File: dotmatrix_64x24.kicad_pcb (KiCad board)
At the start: 2 copper layers, 165.1 x 91.4 mm, 191 parts, among them CON1 BARREL_JACK, P1 CONN_01X09, P2 CONN_01X09, P3 CONN_01X04, P4 CONN_01X03, Q1 NJL7302L-F3, SW1 SW_PUSH_SMALL_H, SW2 SW_PUSH_SMALL_H, SW3 SW_PUSH_SMALL_H, SW4 SW_PUSH_SMALL_H, SW5 SW_PUSH_SMALL_H, SW6 SW_PUSH_SMALL_H, SW7 SW_PUSH_SMALL_H, SW8 SW_PUSH_SMALL_H, U1 WROOM-02, U10 LED1642GW, U11 LED1642GW, U12 AE-BME280, U2 74HC595-alt-vdd, U3 TD62783, U4 74HC595-alt-vdd, U5 TD62783, U6 LED1642GW, U7 74HC595-alt-vdd, U8 TD62783, U9 LED1642GW

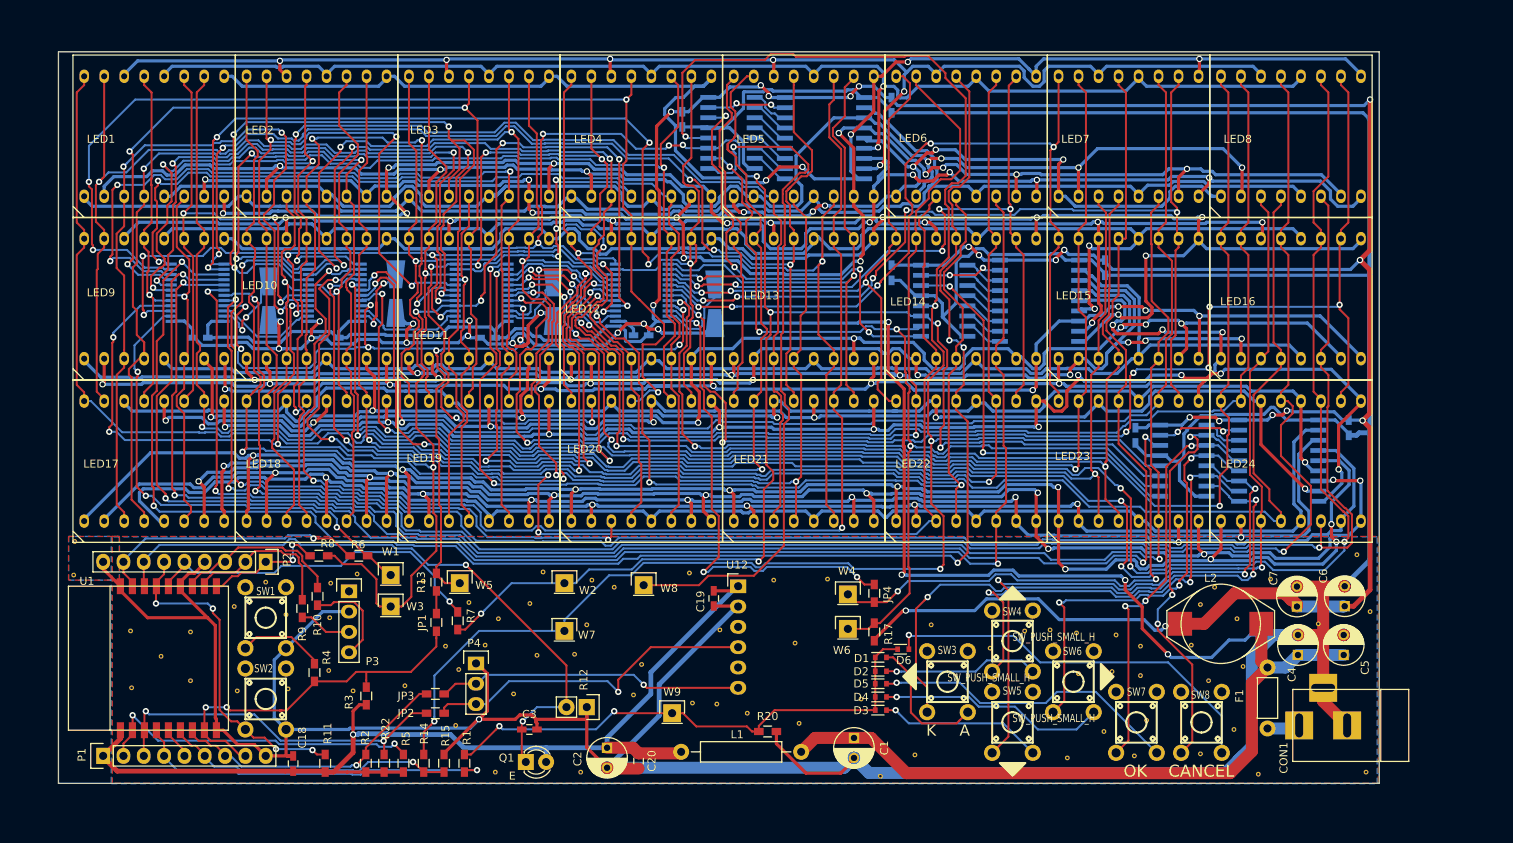
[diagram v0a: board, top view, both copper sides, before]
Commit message: Added DCDC converter to get low power dissipation in LED driver IC
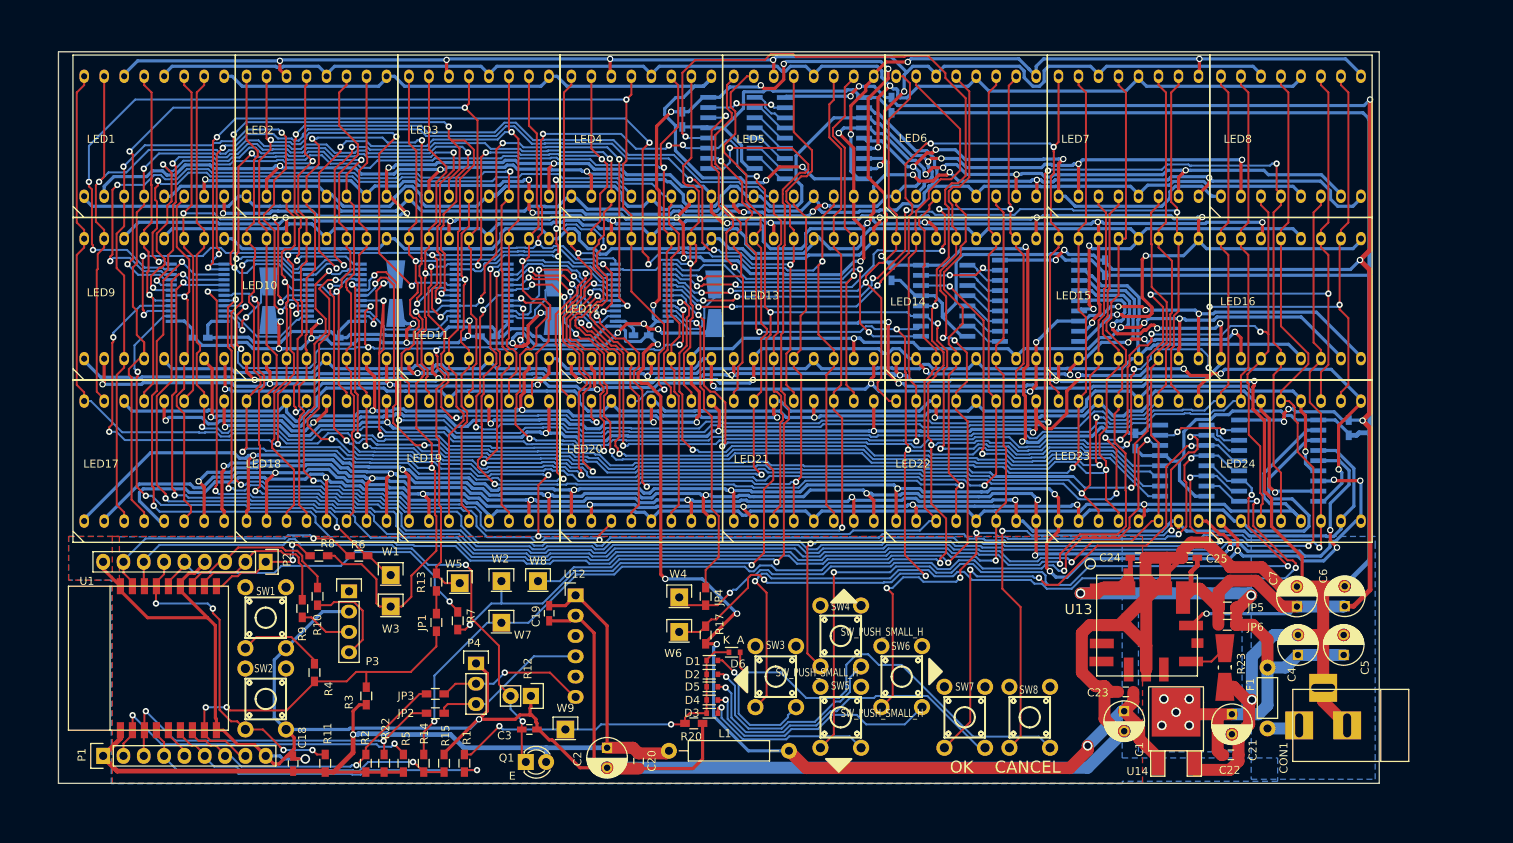
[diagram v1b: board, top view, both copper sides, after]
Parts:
- removed L2: 100uH, Inductors:self_cms_we-pd3
- removed REF** (x77): stitch-via-0.6mm, components:stitch-via-0.6mm
- added C21: 100u, Capacitors_ThroughHole:C_Radial_D5_L6_P2.5, F.Cu at (161.9, 98.0)
- added C22: 1u, Capacitors_SMD:C_0603_HandSoldering, F.Cu at (161.8, 103.1)
- added C23: 1u, Capacitors_SMD:C_0603_HandSoldering, F.Cu at (148.7, 95.2)
- added C24: 1u, Capacitors_SMD:C_0603_HandSoldering, F.Cu at (150.2, 78.5)
- added C25: 1u, Capacitors_SMD:C_0603_HandSoldering, F.Cu at (156.7, 78.5)
- added JP5: Jumper_NO_Small, Resistors_SMD:R_0603_HandSoldering, F.Cu at (161.4, 84.7)
- added JP6: Jumper_NO_Small, Resistors_SMD:R_0603_HandSoldering, F.Cu at (161.3, 86.9)
- added R23: R, Resistors_Universal:Resistor_SMDuniversal_0805to1206_HandSoldering, F.Cu at (161.0, 92.2)
- added U13: OKL-T/6-W5, components:murata-OKL, F.Cu at (151.4, 87.0)
- added U14: NJU7223, TO_SOT_Packages_SMD:TO-252-2Lead, F.Cu at (154.9, 104.1)
- moved C1 33.9 mm to (148.5, 97.7)
- moved SW3 21.5 mm to (102.4, 89.5)
- moved SW4 21.5 mm to (110.5, 84.5)
- moved SW5 21.5 mm to (110.5, 94.6)
- moved SW6 21.5 mm to (118.1, 89.5)
- moved SW7 21.5 mm to (126.0, 94.6)
- moved SW8 21.5 mm to (134.1, 94.6)
- moved D1 21.1 mm to (97.0, 91.3)
- moved D2 21.1 mm to (97.0, 93.0)
- moved D3 21.1 mm to (97.0, 97.9)
- moved D4 21.1 mm to (97.0, 96.3)
- moved D5 21.1 mm to (97.0, 94.6)
- moved JP4 21.1 mm to (96.1, 83.3)
- moved R17 21.1 mm to (96.1, 88.1)
- moved D6 21.1 mm to (99.8, 90.3)
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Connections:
- C1 pad 1: VCC -> /LEDLOGICVDD
- C10 pad 1: /Sheet57A04605/LEDVDD -> /LEDLOGICVDD
- C11 pad 1: /Sheet57A04605/LEDVDD -> /LEDLOGICVDD
- C13 pad 1: /Sheet57A04605/LEDVDD -> /LEDLOGICVDD
- C14 pad 1: /Sheet57A04605/LEDVDD -> /LEDLOGICVDD
- C16 pad 1: /Sheet57A04605/LEDVDD -> /LEDLOGICVDD
- C8 pad 1: /Sheet57A04605/LEDVDD -> /LEDLOGICVDD
- C9 pad 1: /Sheet57A04605/LEDVDD -> /LEDLOGICVDD
- L1 pad 1: VCC -> /LEDLOGICVDD
- R17 pad 1: /Sheet57A04605/LEDVDD -> /LEDLOGICVDD
- U10 pad 24: /Sheet57A04605/LEDVDD -> /LEDLOGICVDD
- U11 pad 24: /Sheet57A04605/LEDVDD -> /LEDLOGICVDD
- U2 pad 16: /Sheet57A04605/LEDVDD -> /LEDLOGICVDD
- U4 pad 16: /Sheet57A04605/LEDVDD -> /LEDLOGICVDD
- U6 pad 24: /Sheet57A04605/LEDVDD -> /LEDLOGICVDD
- U7 pad 16: /Sheet57A04605/LEDVDD -> /LEDLOGICVDD
- U9 pad 24: /Sheet57A04605/LEDVDD -> /LEDLOGICVDD
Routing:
- net /LEDLOGICVDD: track 0.00 -> 353.5 mm, vias 0 -> 13
- net /Sheet57A04605/LEDVDD: track 419.9 -> 253.6 mm, vias 19 -> 10
- net GND: track 825.6 -> 892.9 mm, vias 18 -> 19
- net /Sheet57A04605/SEL1: track 75.8 -> 106.3 mm
- net /Sheet57A04605/c59: track 170.0 -> 200.1 mm, vias 2 -> 5
- net /Sheet57A04605/SEL3: track 73.9 -> 101.8 mm
- net /Sheet57A04605/SEL2: track 58.6 -> 86.1 mm
- net /Sheet57A04605/HC595RESET: track 124.4 -> 149.5 mm, vias 4 -> 6
- net /Sheet57A04605/BUTTONSENSE: track 66.3 -> 43.0 mm
- net /SDA: track 42.6 -> 19.8 mm, vias 1 -> 0
- net /Sheet57A04605/SEL4: track 54.2 -> 75.5 mm, vias 3 -> 5
- net /Sheet57A04605/COLSEROUT: track 60.1 -> 39.1 mm, vias 3 -> 1
- net /Sheet57A04605/SEL5: track 50.8 -> 70.3 mm
- net /SCL: track 38.4 -> 18.9 mm
- net /Sheet57A04605/SEL6: track 52.3 -> 71.4 mm
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- added copper zone on B.Cu, net VCC

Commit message: Added mounting holes, DS1207+ RTC, and more
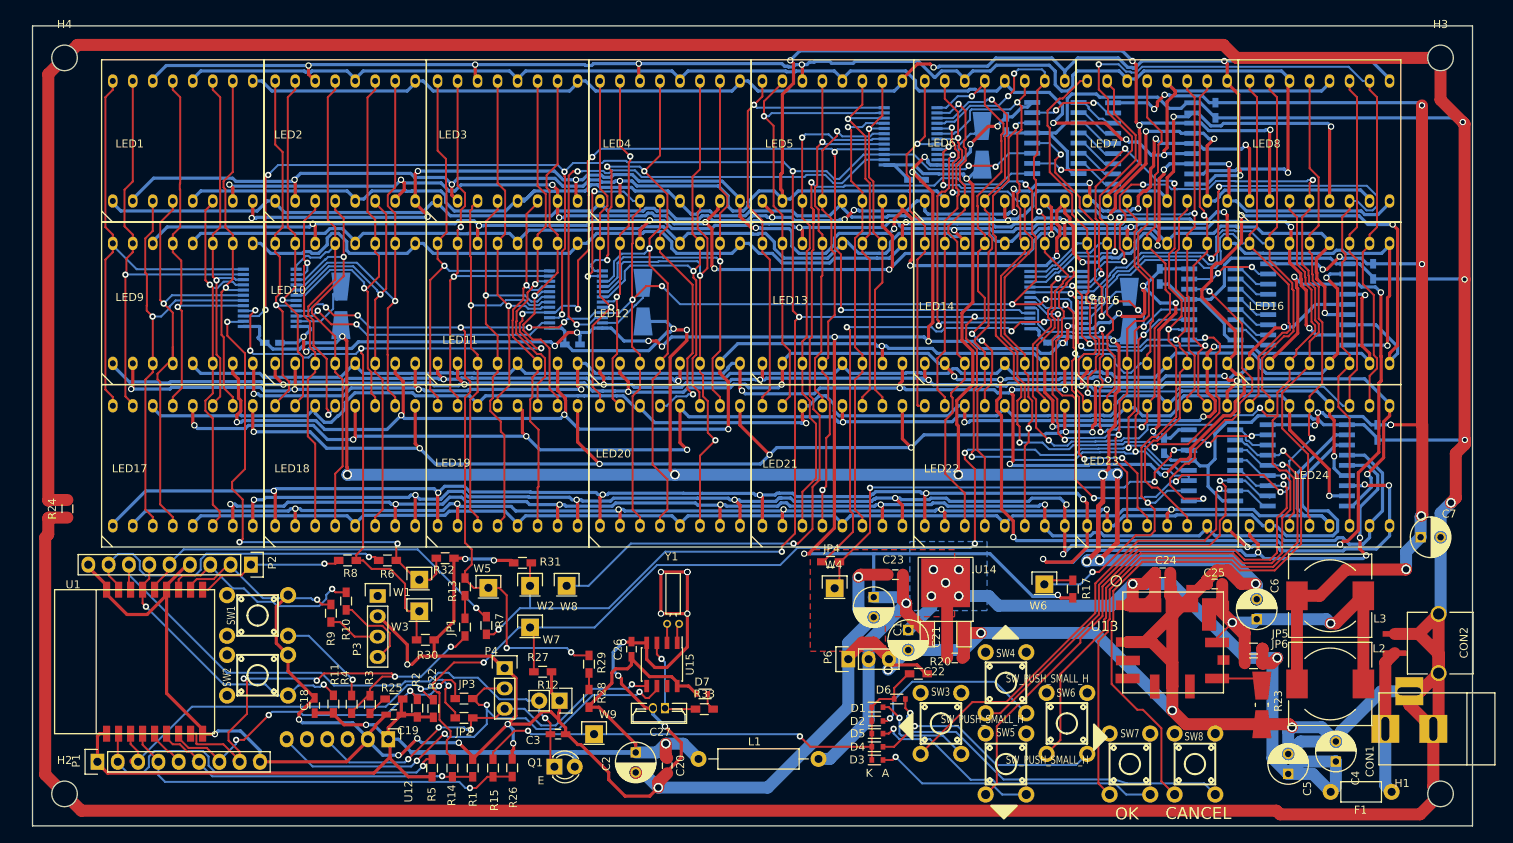
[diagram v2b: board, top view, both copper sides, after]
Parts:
- added C26: 1u, Capacitors_SMD:C_0603_HandSoldering, F.Cu at (86.9, 89.9)
- added C27: 0.22F, components:DCK_614, F.Cu at (91.1, 97.3)
- added CON2: MRUSB-2B, components:MRUSB-2B, F.Cu at (188.1, 89.2)
- added D7: D_Schottky_Small, Diodes_SMD:SOD-523, F.Cu at (95.7, 95.5)
- added H1: TEST_1P, Mounting_Holes:MountingHole_3.2mm_M3, F.Cu at (188.0, 108.0)
- added H2: TEST_1P, Mounting_Holes:MountingHole_3.2mm_M3, F.Cu at (16.0, 108.0)
- added H3: TEST_1P, Mounting_Holes:MountingHole_3.2mm_M3, F.Cu at (188.0, 16.0)
- added H4: TEST_1P, Mounting_Holes:MountingHole_3.2mm_M3, F.Cu at (16.0, 16.0)
- added L2: L_Small, Choke_SMD:Choke_SMD_10.4x10.4_H4.8, F.Cu at (174.2, 94.3)
- added L3: L_Small, Choke_SMD:Choke_SMD_10.4x10.4_H4.8, F.Cu at (174.2, 83.2)
- added P6: CONN_01X03, Pin_Headers:Pin_Header_Straight_1x03, F.Cu at (114.0, 91.2)
- added R24: 120R, Resistors_SMD:R_0603_HandSoldering, F.Cu at (16.4, 72.4)
- added R25: 10k, Resistors_SMD:R_0603_HandSoldering, F.Cu at (57.2, 96.1)
- added R26: 10k, Resistors_SMD:R_0603_HandSoldering, F.Cu at (72.0, 104.7)
- added R27: 10k, Resistors_SMD:R_0603_HandSoldering, F.Cu at (75.8, 92.7)
- added R28: 10k, Resistors_SMD:R_0603_HandSoldering, F.Cu at (81.6, 96.1)
- added R29: 10k, Resistors_SMD:R_0603_HandSoldering, F.Cu at (81.6, 91.8)
- added R30: 10k, Resistors_SMD:R_0603_HandSoldering, F.Cu at (61.1, 88.7)
- added R31: 10k, Resistors_SMD:R_0603_HandSoldering, F.Cu at (73.2, 79.1)
- added R32: 10k, Resistors_SMD:R_0603_HandSoldering, F.Cu at (63.6, 78.5)
- added R33: 120R, Resistors_SMD:R_0603_HandSoldering, F.Cu at (96.0, 97.4)
- added U15: DS1307, Housings_SOIC:SOIC-8_3.9x4.9mm_Pitch1.27mm, F.Cu at (90.7, 91.8)
- added Y1: Crystal_Small, Crystals:Crystal_Round_Horizontal_2mm, F.Cu at (92.1, 86.7)
- D1, D2, D3, D4, D5, D6: value ZENERsmall -> D_Schottky_Small
- moved C11 57.1 mm to (122.5, 31.2)
- moved U10 57.1 mm to (121.8, 25.8)
- moved R19 57.1 mm to (130.7, 26.9)
- moved C10 51.8 mm to (139.9, 51.6)
- moved R21 51.8 mm to (149.1, 47.7)
- moved U11 51.8 mm to (140.0, 46.3)
- moved R17 46.3 mm to (142.0, 82.4)
- moved W6 46.0 mm to (138.5, 81.8)
- moved C21 41.8 mm to (121.5, 87.5)
- moved U3 41.0 mm to (152.0, 26.7)
- moved C12 40.5 mm to (159.9, 22.5)
- moved C14 40.5 mm to (133.7, 24.3)
- moved U2 40.5 mm to (139.9, 26.0)
- moved C22 36.6 mm to (127.3, 91.0)
- moved C1 34.4 mm to (117.1, 83.4)
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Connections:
- C25 pad 1: /Sheet57A04605/LEDVDD -> Net-(C25-Pad1)
- C6 pad 1: /Sheet57A04605/LEDVDD -> Net-(C25-Pad1)
- JP5 pad 2: /Sheet57A04605/LEDVDD -> Net-(C25-Pad1)
- JP6 pad 2: /Sheet57A04605/LEDVDD -> Net-(C25-Pad1)
- R3 pad 1: /ESPVDD -> Net-(R25-Pad2)
- U10 pad 10: /Sheet57A04605/c23 -> /Sheet57A04605/c38
- U10 pad 11: /Sheet57A04605/c27 -> /Sheet57A04605/c39
- U10 pad 12: /Sheet57A04605/c31 -> /Sheet57A04605/c40
- U10 pad 13: /Sheet57A04605/c35 -> /Sheet57A04605/c41
- U10 pad 14: /Sheet57A04605/c39 -> /Sheet57A04605/c42
- U10 pad 16: /Sheet57A04605/c47 -> /Sheet57A04605/c44
- U10 pad 17: /Sheet57A04605/c51 -> /Sheet57A04605/c45
- U10 pad 18: /Sheet57A04605/c55 -> /Sheet57A04605/c46
- U10 pad 19: /Sheet57A04605/c59 -> /Sheet57A04605/c47
- U10 pad 20: /Sheet57A04605/c63 -> /Sheet57A04605/c48
- U10 pad 5: /Sheet57A04605/c3 -> /Sheet57A04605/c33
- U10 pad 6: /Sheet57A04605/c7 -> /Sheet57A04605/c34
- U10 pad 7: /Sheet57A04605/c11 -> /Sheet57A04605/c35
- U10 pad 8: /Sheet57A04605/c15 -> /Sheet57A04605/c36
- U10 pad 9: /Sheet57A04605/c19 -> /Sheet57A04605/c37
- U11 pad 10: /Sheet57A04605/c24 -> /Sheet57A04605/c54
- U11 pad 11: /Sheet57A04605/c28 -> /Sheet57A04605/c55
- U11 pad 12: /Sheet57A04605/c32 -> /Sheet57A04605/c56
- U11 pad 13: /Sheet57A04605/c36 -> /Sheet57A04605/c57
- U11 pad 14: /Sheet57A04605/c40 -> /Sheet57A04605/c58
- U11 pad 15: /Sheet57A04605/c44 -> /Sheet57A04605/c59
- U11 pad 16: /Sheet57A04605/c48 -> /Sheet57A04605/c60
- U11 pad 17: /Sheet57A04605/c52 -> /Sheet57A04605/c61
- U11 pad 18: /Sheet57A04605/c56 -> /Sheet57A04605/c62
- U11 pad 19: /Sheet57A04605/c60 -> /Sheet57A04605/c63
- U11 pad 5: /Sheet57A04605/c4 -> /Sheet57A04605/c49
- U11 pad 6: /Sheet57A04605/c8 -> /Sheet57A04605/c50
- U11 pad 7: /Sheet57A04605/c12 -> /Sheet57A04605/c51
- U11 pad 8: /Sheet57A04605/c16 -> /Sheet57A04605/c52
- U11 pad 9: /Sheet57A04605/c20 -> /Sheet57A04605/c53
- U13 pad 4: /Sheet57A04605/LEDVDD -> Net-(C25-Pad1)
- U13 pad 5: /Sheet57A04605/LEDVDD -> Net-(C25-Pad1)
- U6 pad 10: /Sheet57A04605/c21 -> /Sheet57A04605/c6
- U6 pad 11: /Sheet57A04605/c25 -> /Sheet57A04605/c7
- U6 pad 12: /Sheet57A04605/c29 -> /Sheet57A04605/c8
- U6 pad 13: /Sheet57A04605/c33 -> /Sheet57A04605/c9
- U6 pad 14: /Sheet57A04605/c37 -> /Sheet57A04605/c10
- U6 pad 15: /Sheet57A04605/c41 -> /Sheet57A04605/c11
- U6 pad 16: /Sheet57A04605/c45 -> /Sheet57A04605/c12
- U6 pad 17: /Sheet57A04605/c49 -> /Sheet57A04605/c13
- U6 pad 18: /Sheet57A04605/c53 -> /Sheet57A04605/c14
- U6 pad 19: /Sheet57A04605/c57 -> /Sheet57A04605/c15
- U6 pad 20: /Sheet57A04605/c61 -> /Sheet57A04605/c16
- U6 pad 6: /Sheet57A04605/c5 -> /Sheet57A04605/c2
- U6 pad 7: /Sheet57A04605/c9 -> /Sheet57A04605/c3
- U6 pad 8: /Sheet57A04605/c13 -> /Sheet57A04605/c4
- U6 pad 9: /Sheet57A04605/c17 -> /Sheet57A04605/c5
- U9 pad 11: /Sheet57A04605/c26 -> /Sheet57A04605/c23
- U9 pad 12: /Sheet57A04605/c30 -> /Sheet57A04605/c24
- U9 pad 13: /Sheet57A04605/c34 -> /Sheet57A04605/c25
- U9 pad 14: /Sheet57A04605/c38 -> /Sheet57A04605/c26
- U9 pad 15: /Sheet57A04605/c42 -> /Sheet57A04605/c27
- U9 pad 16: /Sheet57A04605/c46 -> /Sheet57A04605/c28
- U9 pad 17: /Sheet57A04605/c50 -> /Sheet57A04605/c29
- U9 pad 18: /Sheet57A04605/c54 -> /Sheet57A04605/c30
- U9 pad 19: /Sheet57A04605/c58 -> /Sheet57A04605/c31
- U9 pad 20: /Sheet57A04605/c62 -> /Sheet57A04605/c32
- U9 pad 5: /Sheet57A04605/c2 -> /Sheet57A04605/c17
- U9 pad 6: /Sheet57A04605/c6 -> /Sheet57A04605/c18
- U9 pad 7: /Sheet57A04605/c10 -> /Sheet57A04605/c19
- U9 pad 8: /Sheet57A04605/c14 -> /Sheet57A04605/c20
- U9 pad 9: /Sheet57A04605/c18 -> /Sheet57A04605/c21
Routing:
- net GND: track 892.9 -> 1520.8 mm, vias 19 -> 41
- net /Sheet57A04605/c41: track 211.5 -> 53.9 mm, vias 5 -> 3
- net /Sheet57A04605/c49: track 220.6 -> 77.7 mm
- net /Sheet57A04605/c62: track 225.8 -> 91.3 mm, vias 5 -> 2
- net /Sheet57A04605/c45: track 192.2 -> 64.4 mm
- net /Sheet57A04605/c53: track 197.4 -> 72.6 mm
- net /Sheet57A04605/c61: track 215.0 -> 96.7 mm, vias 3 -> 2
- net /Sheet57A04605/c57: track 232.4 -> 115.9 mm, vias 3 -> 5
- net /Sheet57A04605/c26: track 175.6 -> 61.5 mm, vias 6 -> 2
- net /Sheet57A04605/c38: track 162.1 -> 48.2 mm, vias 3 -> 1
- net /Sheet57A04605/c59: track 200.1 -> 89.5 mm, vias 5 -> 3
- net /Sheet57A04605/c46: track 161.0 -> 56.8 mm, vias 3 -> 1
- net /Sheet57A04605/c37: track 157.7 -> 56.9 mm, vias 5 -> 1
- net /Sheet57A04605/c42: track 159.9 -> 60.9 mm, vias 4 -> 1
- net /Sheet57A04605/c58: track 201.7 -> 103.4 mm, vias 7 -> 3
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- added copper zone on F.Cu, net VCC
- removed copper zone on B.Cu, net GND
- removed copper zone on F.Cu, net GND
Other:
- board size 165.1 x 91.4 mm -> 180 x 100 mm
